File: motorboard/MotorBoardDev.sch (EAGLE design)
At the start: 64 parts, among them J1 Under Glow, J2 B2PS-VH(LF)(SN), J3 B2PS-VH(LF)(SN), J4 B2PS-VH(LF)(SN), Q1 SSM3J338R, Q2 SSM3J338R, Q3 SSM3J338R, Q4 STT4P3LLH6, U1 TXB0104DR, U2 9DoF IMU, U3 TXB0106PWR, U4 TLV70233DBVR, X1 C-GRID-05-15-91, X2 C-GRID-05-15-91, X3 MINI-USB_SHIELD5P4-32005-400, X4 C-GRID-02-70553, X5 SI-50170, X7 2510-, X8 2510-

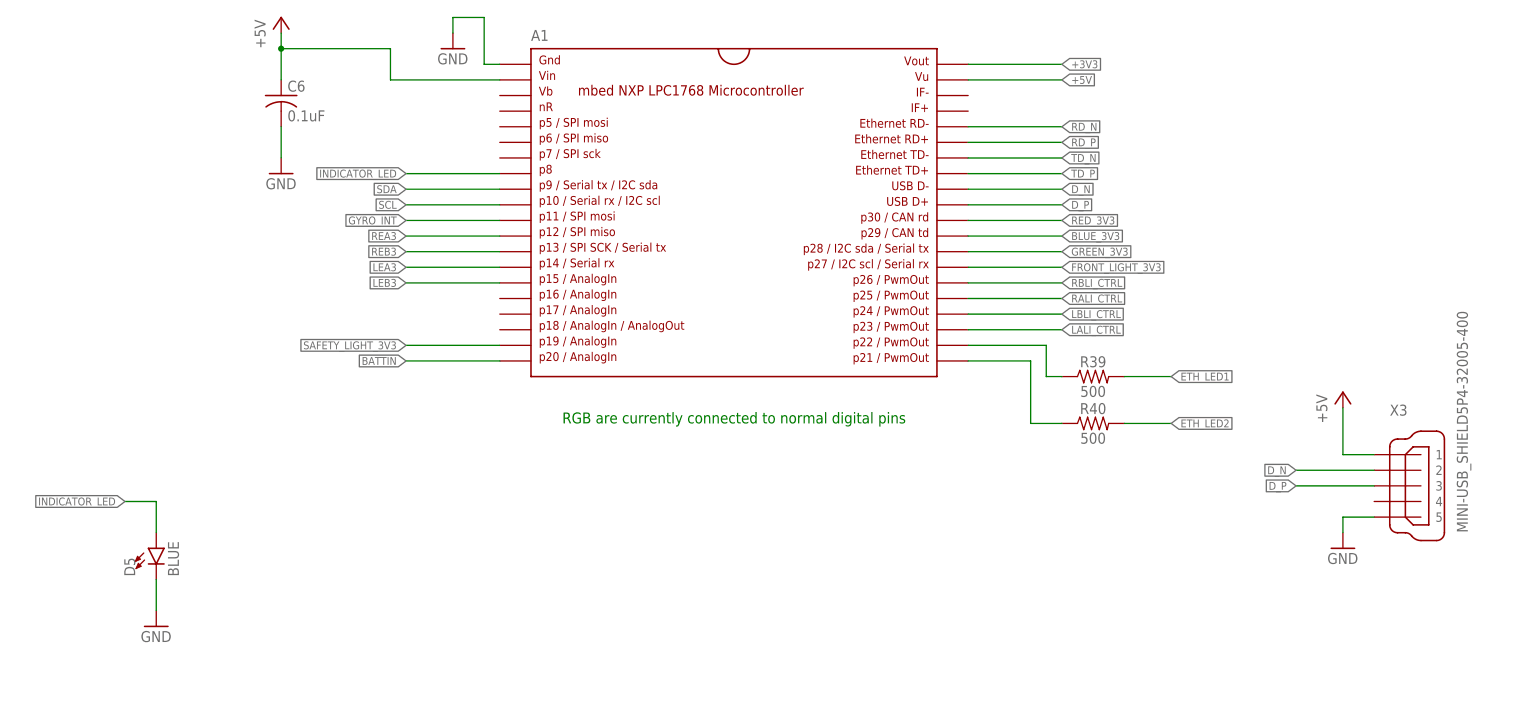
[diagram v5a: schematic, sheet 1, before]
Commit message: Routing Finished, differential pair and silkscreen still need to be fixed.
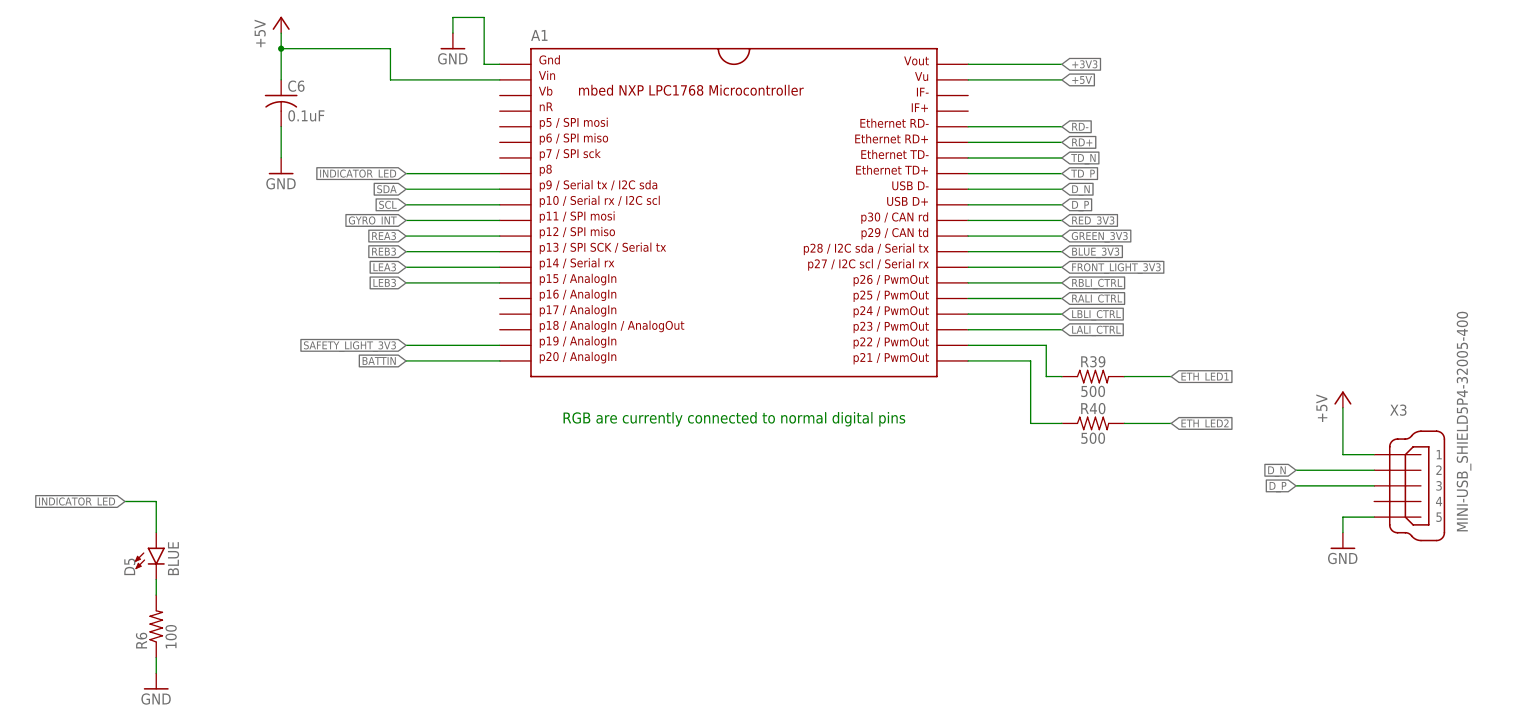
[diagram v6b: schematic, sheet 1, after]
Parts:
- added R6: 100, rcl:R-US_R0603
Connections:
- net RD_N renamed RD-
- net RD_P renamed RD+
- new net N$3: D5.C, R6.2
- net BLUE_3V3: now also A1.P$28; no longer A1.P$29
- net GND: now also R6.1; no longer D5.C
- net GREEN_3V3: now also A1.P$29; no longer A1.P$28
- net LEA: now also U1.A2; no longer U1.A1
- net LEA3: now also U1.B2; no longer U1.B1
- net LEB: now also U1.A1; no longer U1.A2
- net LEB3: now also U1.B1; no longer U1.B2
- net REA: now also U1.A4; no longer U1.A3
- net REA3: now also U1.B4; no longer U1.B3
- net REB: now also U1.A3; no longer U1.A4
- net REB3: now also U1.B3; no longer U1.B4
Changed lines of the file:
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@@
 <part name="U4" library="RoboJackets-PowerICs" deviceset="TLV70233" device="DBVR"/>
 <part name="U$9" library="MotorBoardDev" deviceset="R-78E5.0-1.0" device=""/>
+<part name="R6" library="rcl" library_urn="urn:adsk.eagle:library:334" deviceset="R-US_" device="R0603" package3d_urn="urn:adsk.eagle:package:23555/2" value="100"/>
 </parts>
 <sheets>
@@
 <instance part="GND16" gate="1" x="238.76" y="58.42"/>
 <instance part="D5" gate="G$1" x="45.72" y="58.42"/>
-<instance part="GND13" gate="1" x="45.72" y="45.72"/>
+<instance part="GND13" gate="1" x="45.72" y="35.56"/>
+<instance part="R6" gate="G$1" x="45.72" y="45.72" rot="R90"/>
 </instances>
 <busses>
@@
 </segment>
 <segment>
-<pinref part="D5" gate="G$1" pin="C"/>
-<wire x1="45.72" y1="53.34" x2="45.72" y2="48.26" width="0.1524" layer="91"/>
+<pinref part="R6" gate="G$1" pin="1"/>
 <pinref part="GND13" gate="1" pin="GND"/>
+<wire x1="45.72" y1="38.1" x2="45.72" y2="40.64" width="0.1524" layer="91"/>
 </segment>
 </net>
@@
 <pinref part="A1" gate="G$1" pin="P$10"/>
 <label x="86.36" y="114.3" size="1.27" layer="95" rot="R180" xref="yes"/>
-</segment>
-</net>
-<net name="BATTIN" class="0">
-<segment>
-<wire x1="101.6" y1="88.9" x2="86.36" y2="88.9" width="0.1524" layer="91"/>
-<pinref part="A1" gate="G$1" pin="P$20"/>
-<label x="86.36" y="88.9" size="1.27" layer="95" rot="R180" xref="yes"/>
 </segment>
 </net>
@@
 </segment>
 </net>
-<net name="TD_P" class="0">
-<segment>
-<wire x1="177.8" y1="119.38" x2="193.04" y2="119.38" width="0.1524" layer="91"/>
-<pinref part="A1" gate="G$1" pin="P$33"/>
-<label x="193.04" y="119.38" size="1.27" layer="95" xref="yes"/>
-</segment>
-</net>
-<net name="TD_N" class="0">
-<segment>
-<wire x1="177.8" y1="121.92" x2="193.04" y2="121.92" width="0.1524" layer="91"/>
-<pinref part="A1" gate="G$1" pin="P$34"/>
-<label x="193.04" y="121.92" size="1.27" layer="95" xref="yes"/>
-</segment>
-</net>
-<net name="RD_P" class="0">
-<segment>
-<wire x1="177.8" y1="124.46" x2="193.04" y2="124.46" width="0.1524" layer="91"/>
-<pinref part="A1" gate="G$1" pin="P$35"/>
-<label x="193.04" y="124.46" size="1.27" layer="95" xref="yes"/>
-</segment>
-</net>
-<net name="RD_N" class="0">
+<net name="RD-" class="0">
 <segment>
 <wire x1="177.8" y1="127" x2="193.04" y2="127" width="0.1524" layer="91"/>
@@
 </segment>
 </net>
-<net name="BLUE_3V3" class="0">
+<net name="GREEN_3V3" class="0">
 <segment>
 <pinref part="A1" gate="G$1" pin="P$29"/>
@@
 </segment>
 </net>
-<net name="GREEN_3V3" class="0">
+<net name="SAFETY_LIGHT_3V3" class="0">
+<segment>
+<pinref part="A1" gate="G$1" pin="P$19"/>
+<wire x1="101.6" y1="91.44" x2="86.36" y2="91.44" width="0.1524" layer="91"/>
+<label x="86.36" y="91.44" size="1.27" layer="95" rot="R180" xref="yes"/>
+</segment>
+</net>
+<net name="FRONT_LIGHT_3V3" class="0">
+<segment>
+<pinref part="A1" gate="G$1" pin="P$27"/>
+<wire x1="177.8" y1="104.14" x2="193.04" y2="104.14" width="0.1524" layer="91"/>
+<label x="193.04" y="104.14" size="1.27" layer="95" xref="yes"/>
+</segment>
+</net>
+<net name="N$3" class="0">
+<segment>
+<pinref part="D5" gate="G$1" pin="C"/>
+<pinref part="R6" gate="G$1" pin="2"/>
+<wire x1="45.72" y1="50.8" x2="45.72" y2="53.34" width="0.1524" layer="91"/>
+</segment>
+</net>
+<net name="BATTIN" class="0">
+<segment>
+<pinref part="A1" gate="G$1" pin="P$20"/>
+<wire x1="101.6" y1="88.9" x2="86.36" y2="88.9" width="0.1524" layer="91"/>
+<label x="86.36" y="88.9" size="1.27" layer="95" rot="R180" xref="yes"/>
+</segment>
+</net>
+<net name="BLUE_3V3" class="0">
 <segment>
 <pinref part="A1" gate="G$1" pin="P$28"/>
@@
 </segment>
 </net>
-<net name="SAFETY_LIGHT_3V3" class="0">
-<segment>
-<pinref part="A1" gate="G$1" pin="P$19"/>
-<wire x1="101.6" y1="91.44" x2="86.36" y2="91.44" width="0.1524" layer="91"/>
-<label x="86.36" y="91.44" size="1.27" layer="95" rot="R180" xref="yes"/>
-</segment>
-</net>
-<net name="FRONT_LIGHT_3V3" class="0">
-<segment>
-<pinref part="A1" gate="G$1" pin="P$27"/>
-<wire x1="177.8" y1="104.14" x2="193.04" y2="104.14" width="0.1524" layer="91"/>
-<label x="193.04" y="104.14" size="1.27" layer="95" xref="yes"/>
+<net name="RD+" class="0">
+<segment>
+<wire x1="177.8" y1="124.46" x2="193.04" y2="124.46" width="0.1524" layer="91"/>
+<pinref part="A1" gate="G$1" pin="P$35"/>
+<label x="193.04" y="124.46" size="1.27" layer="95" xref="yes"/>
+</segment>
+</net>
+<net name="TD_N" class="0">
+<segment>
+<wire x1="177.8" y1="121.92" x2="193.04" y2="121.92" width="0.1524" layer="91"/>
+<pinref part="A1" gate="G$1" pin="P$34"/>
+<label x="193.04" y="121.92" size="1.27" layer="95" xref="yes"/>
+</segment>
+</net>
+<net name="TD_P" class="0">
+<segment>
+<wire x1="177.8" y1="119.38" x2="193.04" y2="119.38" width="0.1524" layer="91"/>
+<pinref part="A1" gate="G$1" pin="P$33"/>
+<label x="193.04" y="119.38" size="1.27" layer="95" xref="yes"/>
 </segment>
 </net>
@@
 </segment>
 </net>
-<net name="RD_N" class="0">
+<net name="RD-" class="0">
 <segment>
 <pinref part="X5" gate="G$1" pin="RD-"/>
@@
 </segment>
 </net>
-<net name="RD_P" class="0">
+<net name="RD+" class="0">
 <segment>
 <pinref part="X5" gate="G$1" pin="RD+"/>
@@
 </segment>
 </net>
-<net name="LEA" class="0">
+<net name="LEB" class="0">
 <segment>
 <pinref part="U1" gate="A" pin="A1"/>
@@
 </segment>
 </net>
-<net name="LEB" class="0">
-<segment>
-<pinref part="U1" gate="A" pin="A2"/>
-<wire x1="35.56" y1="111.76" x2="27.305" y2="111.76" width="0.1524" layer="91"/>
-<label x="27.305" y="111.76" size="1.27" layer="95" rot="R180" xref="yes"/>
-</segment>
-</net>
-<net name="REA" class="0">
+<net name="REB" class="0">
 <segment>
 <pinref part="U1" gate="A" pin="A3"/>
 <wire x1="35.56" y1="109.22" x2="27.305" y2="109.22" width="0.1524" layer="91"/>
 <label x="27.305" y="109.22" size="1.27" layer="95" rot="R180" xref="yes"/>
-</segment>
-</net>
-<net name="REB" class="0">
-<segment>
-<pinref part="U1" gate="A" pin="A4"/>
-<wire x1="35.56" y1="106.68" x2="27.305" y2="106.68" width="0.1524" layer="91"/>
-<label x="27.305" y="106.68" size="1.27" layer="95" rot="R180" xref="yes"/>
 </segment>
 </net>
@@
 <net name="LEB3" class="0">
 <segment>
-<pinref part="U1" gate="A" pin="B2"/>
-<wire x1="91.44" y1="111.76" x2="99.06" y2="111.76" width="0.1524" layer="91"/>
-<label x="99.06" y="111.76" size="1.27" layer="95" xref="yes"/>
-</segment>
-</net>
-<net name="LEA3" class="0">
-<segment>
 <pinref part="U1" gate="A" pin="B1"/>
 <wire x1="91.44" y1="114.3" x2="99.06" y2="114.3" width="0.1524" layer="91"/>
@@
 </segment>
 </net>
-<net name="REA3" class="0">
+<net name="REB3" class="0">
 <segment>
 <pinref part="U1" gate="A" pin="B3"/>
 <wire x1="91.44" y1="109.22" x2="99.06" y2="109.22" width="0.1524" layer="91"/>
 <label x="99.06" y="109.22" size="1.27" layer="95" xref="yes"/>
-</segment>
-</net>
-<net name="REB3" class="0">
-<segment>
-<pinref part="U1" gate="A" pin="B4"/>
-<wire x1="91.44" y1="106.68" x2="99.06" y2="106.68" width="0.1524" layer="91"/>
-<label x="99.06" y="106.68" size="1.27" layer="95" xref="yes"/>
 </segment>
 </net>
@@
 </segment>
 </net>
+<net name="REA" class="0">
+<segment>
+<pinref part="U1" gate="A" pin="A4"/>
+<wire x1="35.56" y1="106.68" x2="27.305" y2="106.68" width="0.1524" layer="91"/>
+<label x="27.305" y="106.68" size="1.27" layer="95" rot="R180" xref="yes"/>
+</segment>
+</net>
+<net name="REA3" class="0">
+<segment>
+<pinref part="U1" gate="A" pin="B4"/>
+<wire x1="91.44" y1="106.68" x2="99.06" y2="106.68" width="0.1524" layer="91"/>
+<label x="99.06" y="106.68" size="1.27" layer="95" xref="yes"/>
+</segment>
+</net>
+<net name="LEA3" class="0">
+<segment>
+<pinref part="U1" gate="A" pin="B2"/>
+<wire x1="91.44" y1="111.76" x2="99.06" y2="111.76" width="0.1524" layer="91"/>
+<label x="99.06" y="111.76" size="1.27" layer="95" xref="yes"/>
+</segment>
+</net>
+<net name="LEA" class="0">
+<segment>
+<pinref part="U1" gate="A" pin="A2"/>
+<wire x1="35.56" y1="111.76" x2="27.305" y2="111.76" width="0.1524" layer="91"/>
+<label x="27.305" y="111.76" size="1.27" layer="95" rot="R180" xref="yes"/>
+</segment>
+</net>
